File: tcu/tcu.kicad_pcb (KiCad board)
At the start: 2 copper layers, 52 parts, among them CON1 USB-MICRO-B, K1 SPDT_RELAY, K2 SPDT_RELAY, K3 SPDT_RELAY, P1 CONN_01X08, P2 CONN_02X03, P3 NRF24L01+, P4 ESP8266, Q1 E_NMOS, Q2 E_NMOS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

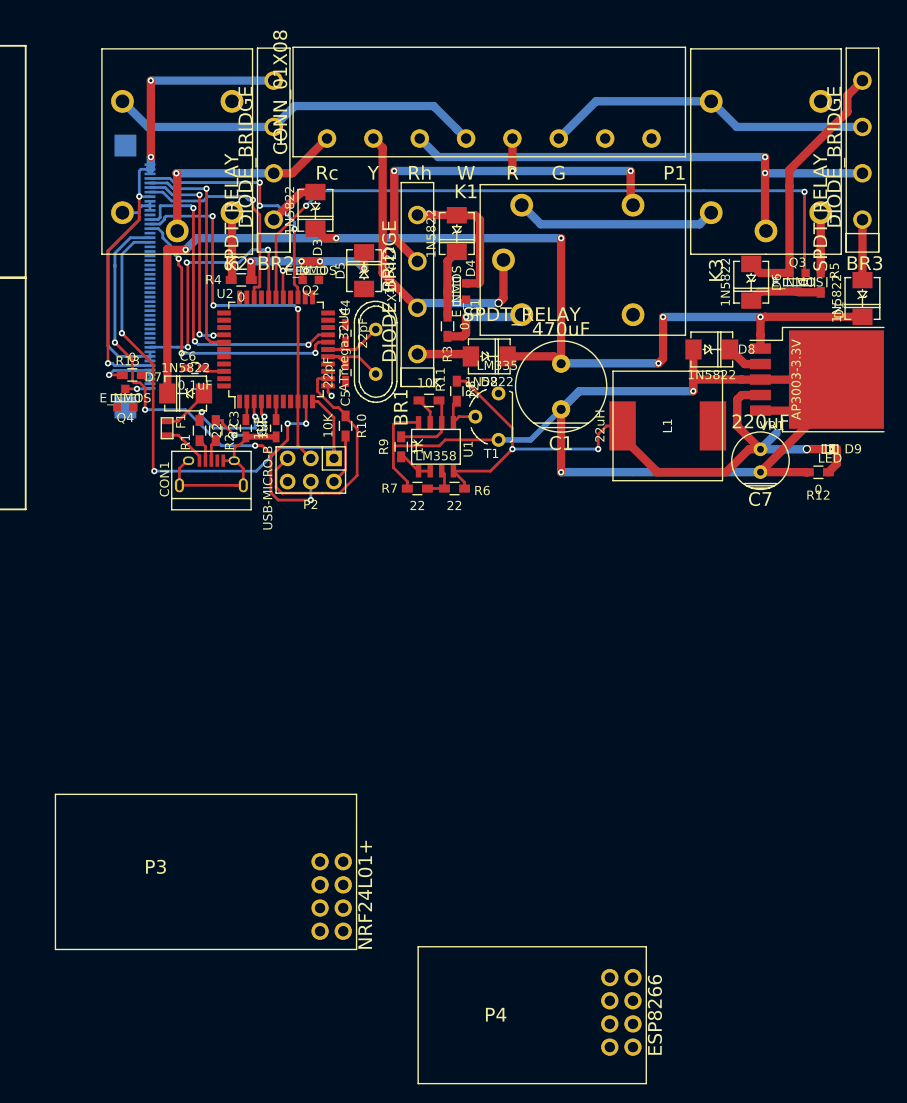
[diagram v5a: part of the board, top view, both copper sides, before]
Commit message: began routing wifi modules
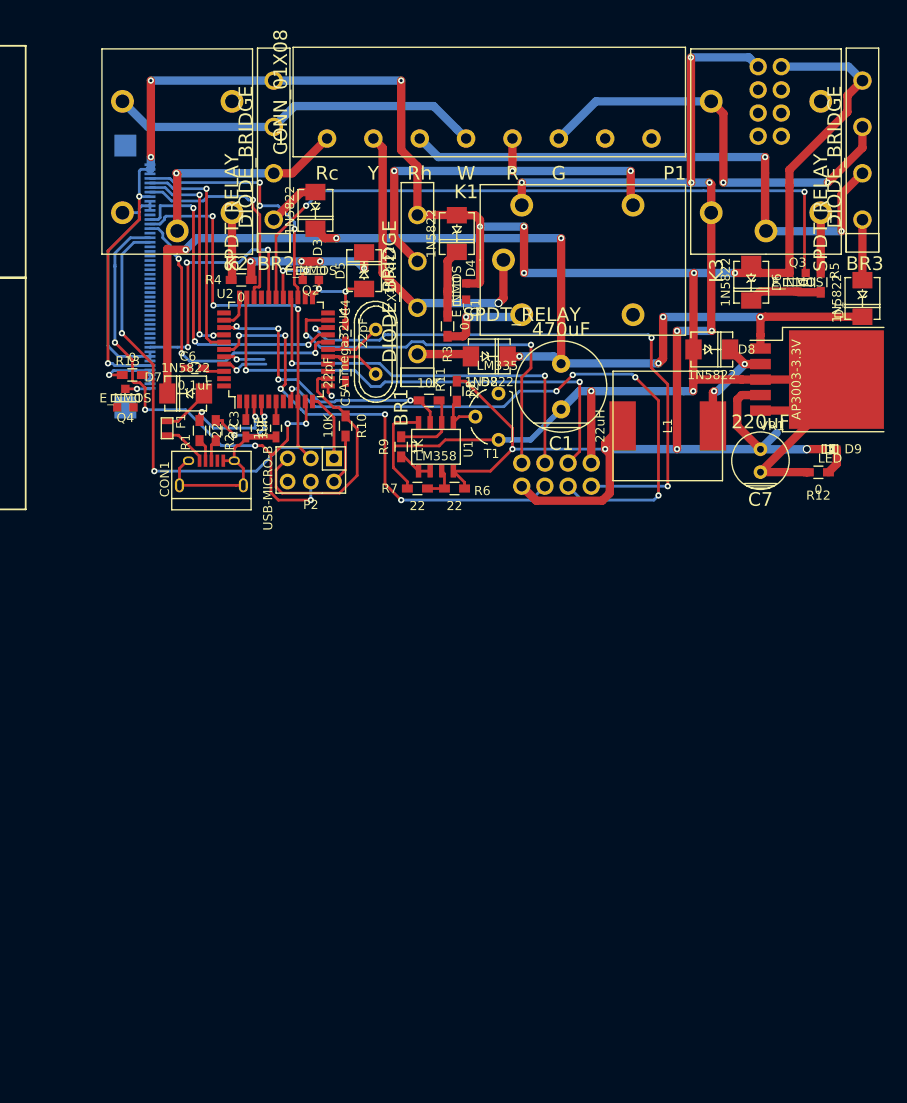
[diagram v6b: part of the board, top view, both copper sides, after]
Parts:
- P3, P4: moved to B.Cu
- moved P3 106.2 mm to (138.7, 22.6)
- moved P4 64.0 mm to (120.4, 66.0), turned to 270 degrees
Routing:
- net GND: track 245.2 -> 322.3 mm, vias 6 -> 14
- net VCC: track 126.8 -> 196.7 mm, vias 3 -> 10
- net /CH_PD: track 0.00 -> 66.3 mm, vias 0 -> 5
- net /TXD: track 0.00 -> 64.6 mm, vias 0 -> 3
- net /GPIO2: track 0.00 -> 55.0 mm, vias 0 -> 2
- net /ESP_RESET: track 0.00 -> 53.1 mm, vias 0 -> 5
- net /GPIO0: track 0.00 -> 45.1 mm, vias 0 -> 2
- net /RXD: track 0.00 -> 43.1 mm, vias 0 -> 2
- net /TEMPERATURE: track 2.92 -> 31.2 mm, vias 0 -> 4
- net Net-(BR3-Pad1): track 36.1 -> 47.0 mm, vias 0 -> 2
- net Net-(D8-Pad2): track 7.31 -> 15.8 mm, vias 0 -> 2
- net /CSN: track 0.00 -> 5.16 mm, vias 0 -> 1
- net Net-(BR3-Pad2): track 57.5 -> 62.4 mm
- net /CE: track 0.00 -> 4.51 mm, vias 0 -> 1
- net /D/C: track 32.7 -> 33.4 mm
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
